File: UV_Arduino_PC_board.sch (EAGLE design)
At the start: 9 parts

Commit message: Added circuit board
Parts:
- removed X4: (no value), con-wago-500:W237-102
- added X5: (no value), con-wago-508:W237-04P
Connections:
- new net N$10: JP1.15, JP2.4
- new net N$12: JP1.8, X5-3.KL
- new net N$13: JP1.7, X5-2.KL
- new net N$2: JP1.14, JP2.5
- new net N$5: JP1.11, X1-1.KL, X2-1.KL
- new net N$6: JP1.10, X2-3.KL
- new net N$7: JP1.9, X2-2.KL
- new net N$8: JP1.6, X1-3.KL
- new net N$9: JP1.5, X1-2.KL
- net +12V: now also JP3.1
- net +5V: now also JP1.16, X5-4.KL
- net GND: now also JP1.1, JP1.17, JP3.2, X5-1.KL
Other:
- note added: "18 - RST 17 - GND 16 - +5VDC 15 - Arduino 0 RX 14 - Arduino 1 TX 13 - Arduino 2 12 - Arduino 3 11 - Arduino 4 Motor ENABLE -> SHB both EA 10 - Arduino 5 Left motor F -> SHB 0 PA 9 - Arduino 6 Left motor R -> SHB 0 PB 8 - Arduino 7 Platform UP / ~DOWN 7 - Arduino 8 Platform motion ENABLE 6 - Arduino 9 Right motor F -> SHB 1 PA 5 - Arduino 10 Right motor R -> SHB 1 PB 4 - Arduino 11 3 - Arduino 12 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"
- note added: "2 - GND 1 - Vin +12VDC to Arduino"
- note added: "BBB Arduino with jumper PRJ set for EXT"
- note added: "INPUT"
- note added: "OUTPUT"
- note added: "Pneumatics Control 4 - +5VDC 3 - UP / ~DOWN 2 - ENABLE 1 - GND"
- note removed: "BBB Arduino with jumper PRJ set for 5V"
- moved on the sheet: JP1, JP2, JP3, X1-1, X1-2, X1-3, X2-1, X2-2, X2-3

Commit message: Added name to schematic
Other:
- note added: "1.0"
- note added: "Author: Charles B. Malloch, PhD"
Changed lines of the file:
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@@
 2 - ENABLE
 1 - GND</text>
+<text x="162.56" y="12.7" size="2.54" layer="94" font="vector">Author: Charles B. Malloch, PhD</text>
+<text x="251.46" y="-7.62" size="2.54" layer="94" font="vector">1.0</text>
 </plain>
 <instances>

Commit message: Changed layout to fit actual board
Added change order to allow for a string of LEDs
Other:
- note added: "Change order: Add a connector for a string of neopixels or other addressable RGB LEDs - comm pins and 12V? power"
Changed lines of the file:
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@@
 <text x="162.56" y="12.7" size="2.54" layer="94" font="vector">Author: Charles B. Malloch, PhD</text>
 <text x="251.46" y="-7.62" size="2.54" layer="94" font="vector">1.0</text>
+<text x="45.72" y="-45.72" size="5.08" layer="94">Change order:
+Add a connector for a string of neopixels or other
+addressable RGB LEDs - comm pins and 12V? power</text>
 </plain>
 <instances>

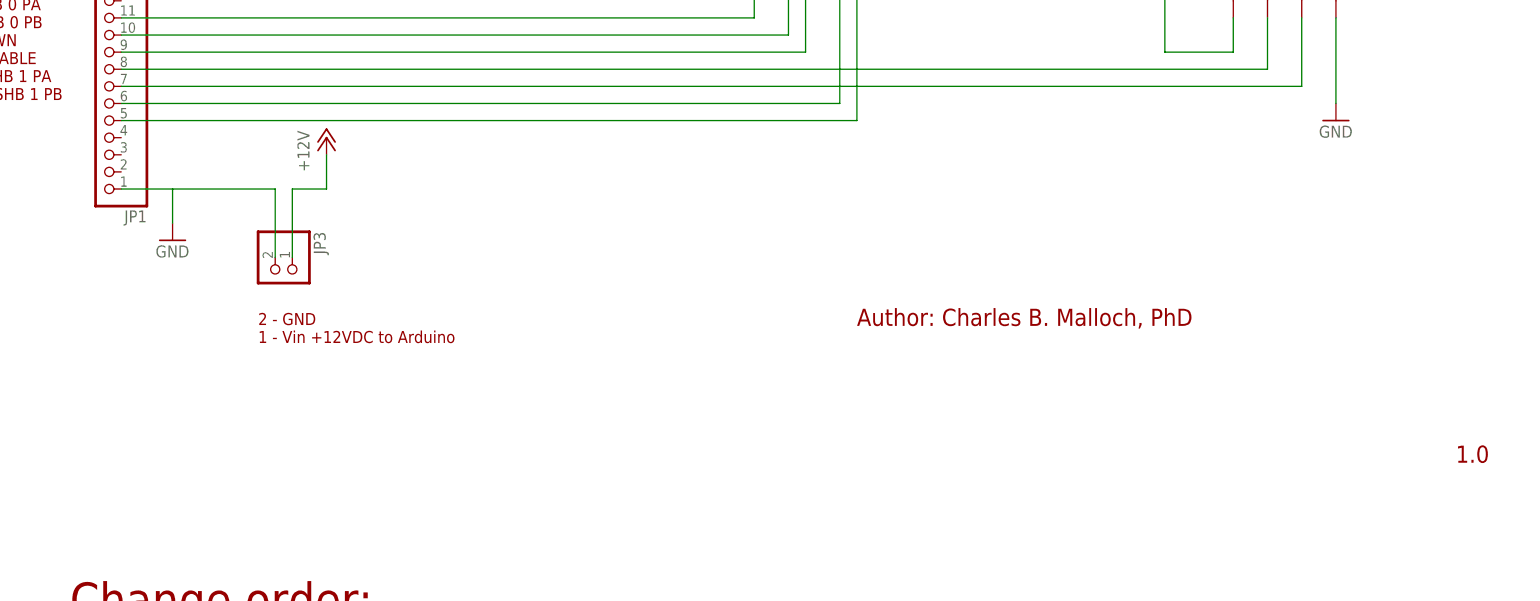
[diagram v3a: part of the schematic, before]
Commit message: Added lights control terminals
to control a LED strip with WS2811 or WS2812 controlled individually
addressable LEDs
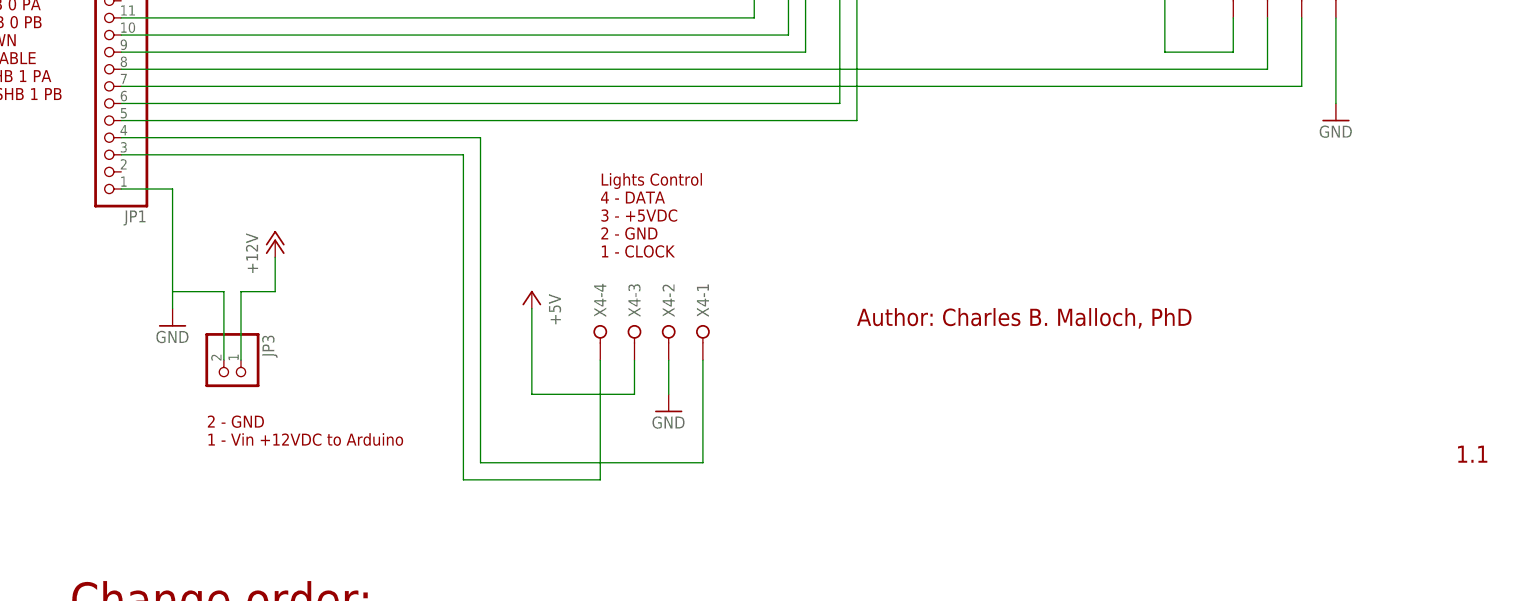
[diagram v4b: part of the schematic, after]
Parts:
- added X4: (no value), con-wago-508:W237-04P
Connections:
- new net N$3: JP1.4, X4-1.KL
- new net N$4: JP1.3, X4-4.KL
- net +5V: now also X4-3.KL
- net GND: now also X4-2.KL
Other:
- note added: "1.1"
- note added: "Lights Control 4 - DATA 3 - +5VDC 2 - GND 1 - CLOCK"
- note removed: "1.0"
- moved on the sheet: JP3
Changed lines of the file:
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@@
 <part name="GND6" library="supply1" deviceset="GND" device=""/>
 <part name="P+6" library="supply1" deviceset="+5V" device=""/>
+<part name="X4" library="con-wago-508" deviceset="W237-04P" device=""/>
+<part name="GND7" library="supply1" deviceset="GND" device=""/>
+<part name="P+7" library="supply1" deviceset="+5V" device=""/>
 </parts>
 <sheets>
@@
   2 - Arduino 13
   1 - GND</text>
-<text x="73.66" y="10.16" size="1.778" layer="94">2 - GND
+<text x="66.04" y="-5.08" size="1.778" layer="94">2 - GND
 1 - Vin +12VDC to Arduino</text>
 <text x="50.8" y="157.48" size="1.778" layer="94">INPUT</text>
@@
 1 - GND</text>
 <text x="162.56" y="12.7" size="2.54" layer="94" font="vector">Author: Charles B. Malloch, PhD</text>
-<text x="251.46" y="-7.62" size="2.54" layer="94" font="vector">1.0</text>
+<text x="251.46" y="-7.62" size="2.54" layer="94" font="vector">1.1</text>
 <text x="45.72" y="-45.72" size="5.08" layer="94">Change order:
 Add a connector for a string of neopixels or other
 addressable RGB LEDs - comm pins and 12V? power</text>
+<text x="124.46" y="22.86" size="1.778" layer="94">Lights Control
+4 - DATA
+3 - +5VDC
+2 - GND
+1 - CLOCK</text>
 </plain>
 <instances>
 <instance part="JP1" gate="A" x="50.8" y="53.34" rot="R180"/>
 <instance part="JP2" gate="A" x="152.4" y="152.4"/>
-<instance part="JP3" gate="G$1" x="76.2" y="20.32" rot="R270"/>
+<instance part="JP3" gate="G$1" x="68.58" y="5.08" rot="R270"/>
 <instance part="X1" gate="-1" x="170.18" y="83.82" rot="R180"/>
 <instance part="X1" gate="-2" x="170.18" y="88.9" rot="R180"/>
@@
 <instance part="GND3" gate="1" x="132.08" y="142.24"/>
 <instance part="P+4" gate="1" x="71.12" y="81.28" rot="MR0"/>
-<instance part="GND4" gate="1" x="60.96" y="25.4"/>
+<instance part="GND4" gate="1" x="60.96" y="12.7"/>
 <instance part="X5" gate="-1" x="233.68" y="63.5" rot="R270"/>
 <instance part="X5" gate="-2" x="228.6" y="63.5" rot="R270"/>
 <instance part="X5" gate="-3" x="223.52" y="63.5" rot="R270"/>
 <instance part="X5" gate="-4" x="218.44" y="63.5" rot="R270"/>
-<instance part="P+5" gate="1" x="83.82" y="40.64"/>
+<instance part="P+5" gate="1" x="76.2" y="25.4"/>
 <instance part="GND5" gate="1" x="66.04" y="76.2"/>
 <instance part="GND6" gate="1" x="233.68" y="43.18"/>
 <instance part="P+6" gate="1" x="208.28" y="68.58" rot="MR0"/>
+<instance part="X4" gate="-1" x="139.7" y="12.7" rot="R270"/>
+<instance part="X4" gate="-2" x="134.62" y="12.7" rot="R270"/>
+<instance part="X4" gate="-3" x="129.54" y="12.7" rot="R270"/>
+<instance part="X4" gate="-4" x="124.46" y="12.7" rot="R270"/>
+<instance part="GND7" gate="1" x="134.62" y="0"/>
+<instance part="P+7" gate="1" x="114.3" y="17.78" rot="MR0"/>
 </instances>
 <busses>
@@
 <pinref part="GND4" gate="1" pin="GND"/>
 <wire x1="53.34" y1="33.02" x2="60.96" y2="33.02" width="0.1524" layer="91"/>
-<wire x1="60.96" y1="33.02" x2="60.96" y2="27.94" width="0.1524" layer="91"/>
+<wire x1="60.96" y1="33.02" x2="60.96" y2="17.78" width="0.1524" layer="91"/>
+<wire x1="60.96" y1="17.78" x2="60.96" y2="15.24" width="0.1524" layer="91"/>
 <pinref part="JP3" gate="G$1" pin="2"/>
-<wire x1="76.2" y1="22.86" x2="76.2" y2="33.02" width="0.1524" layer="91"/>
-<wire x1="76.2" y1="33.02" x2="60.96" y2="33.02" width="0.1524" layer="91"/>
+<wire x1="68.58" y1="7.62" x2="68.58" y2="17.78" width="0.1524" layer="91"/>
+<wire x1="68.58" y1="17.78" x2="60.96" y2="17.78" width="0.1524" layer="91"/>
 </segment>
 <segment>
@@
 <pinref part="GND6" gate="1" pin="GND"/>
 <wire x1="233.68" y1="58.42" x2="233.68" y2="45.72" width="0.1524" layer="91"/>
+</segment>
+<segment>
+<pinref part="X4" gate="-2" pin="KL"/>
+<pinref part="GND7" gate="1" pin="GND"/>
+<wire x1="134.62" y1="7.62" x2="134.62" y2="2.54" width="0.1524" layer="91"/>
 </segment>
 </net>
@@
 <segment>
 <pinref part="JP3" gate="G$1" pin="1"/>
-<wire x1="78.74" y1="22.86" x2="78.74" y2="33.02" width="0.1524" layer="91"/>
+<wire x1="71.12" y1="7.62" x2="71.12" y2="17.78" width="0.1524" layer="91"/>
 <pinref part="P+5" gate="1" pin="+12V"/>
-<wire x1="78.74" y1="33.02" x2="83.82" y2="33.02" width="0.1524" layer="91"/>
-<wire x1="83.82" y1="33.02" x2="83.82" y2="38.1" width="0.1524" layer="91"/>
+<wire x1="71.12" y1="17.78" x2="76.2" y2="17.78" width="0.1524" layer="91"/>
+<wire x1="76.2" y1="17.78" x2="76.2" y2="22.86" width="0.1524" layer="91"/>
 </segment>
 </net>
@@
 <wire x1="218.44" y1="53.34" x2="208.28" y2="53.34" width="0.1524" layer="91"/>
 <wire x1="208.28" y1="53.34" x2="208.28" y2="66.04" width="0.1524" layer="91"/>
+</segment>
+<segment>
+<pinref part="P+7" gate="1" pin="+5V"/>
+<wire x1="114.3" y1="2.54" x2="114.3" y2="15.24" width="0.1524" layer="91"/>
+<pinref part="X4" gate="-3" pin="KL"/>
+<wire x1="114.3" y1="2.54" x2="129.54" y2="2.54" width="0.1524" layer="91"/>
+<wire x1="129.54" y1="2.54" x2="129.54" y2="7.62" width="0.1524" layer="91"/>
 </segment>
 </net>
@@
 </segment>
 </net>
+<net name="N$3" class="0">
+<segment>
+<pinref part="JP1" gate="A" pin="4"/>
+<wire x1="53.34" y1="40.64" x2="106.68" y2="40.64" width="0.1524" layer="91"/>
+<wire x1="106.68" y1="40.64" x2="106.68" y2="-7.62" width="0.1524" layer="91"/>
+<pinref part="X4" gate="-1" pin="KL"/>
+<wire x1="106.68" y1="-7.62" x2="139.7" y2="-7.62" width="0.1524" layer="91"/>
+<wire x1="139.7" y1="-7.62" x2="139.7" y2="7.62" width="0.1524" layer="91"/>
+</segment>
+</net>
+<net name="N$4" class="0">
+<segment>
+<pinref part="JP1" gate="A" pin="3"/>
+<wire x1="53.34" y1="38.1" x2="104.14" y2="38.1" width="0.1524" layer="91"/>
+<wire x1="104.14" y1="38.1" x2="104.14" y2="-10.16" width="0.1524" layer="91"/>
+<pinref part="X4" gate="-4" pin="KL"/>
+<wire x1="104.14" y1="-10.16" x2="124.46" y2="-10.16" width="0.1524" layer="91"/>
+<wire x1="124.46" y1="-10.16" x2="124.46" y2="7.62" width="0.1524" layer="91"/>
+</segment>
+</net>

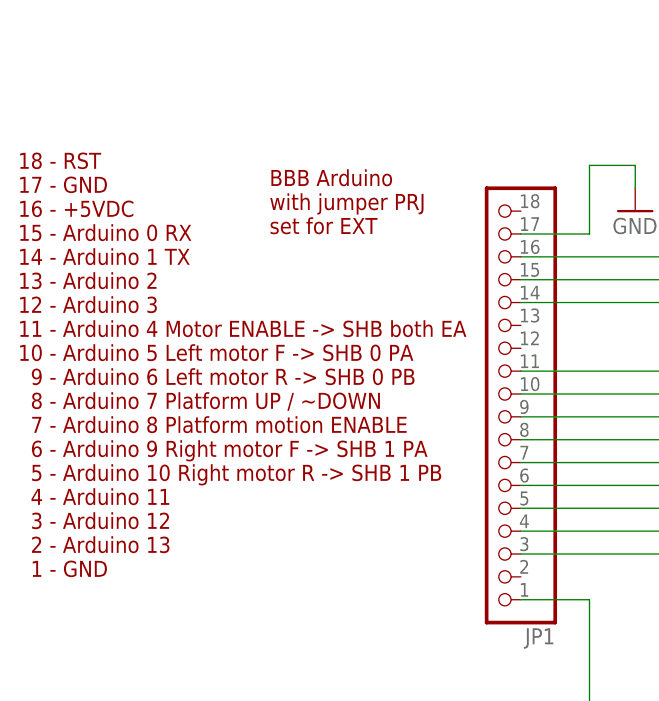
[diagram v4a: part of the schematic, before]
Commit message: Files now in Eagle v7.1.0 format
fixed some comments and adjusted to match the actual build.
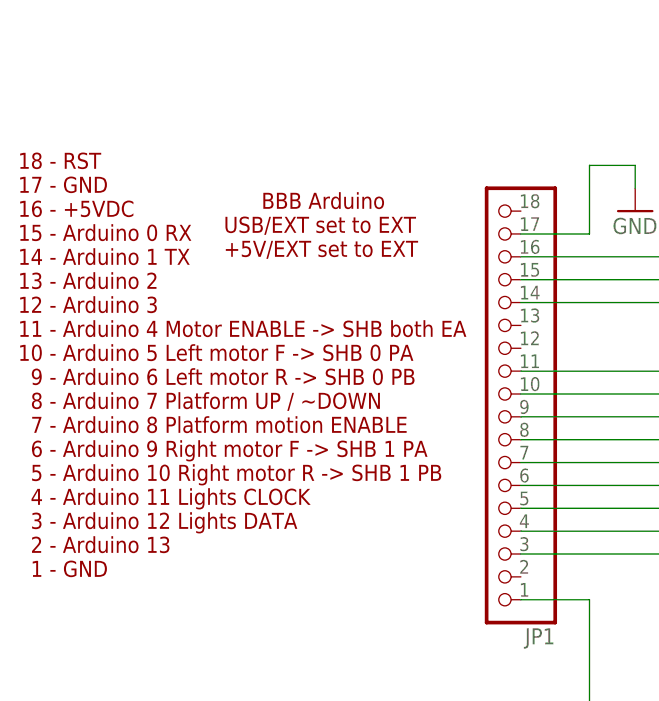
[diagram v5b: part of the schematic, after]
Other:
- note added: "18 - RST 17 - GND 16 - +5VDC 15 - Arduino 0 RX 14 - Arduino 1 TX 13 - Arduino 2 12 - Arduino 3 11 - Arduino 4 Motor ENABLE -> SHB both EA 10 - Arduino 5 Left motor F -> SHB 0 PA 9 - Arduino 6 Left motor R -> SHB 0 PB 8 - Arduino 7 Platform UP / ~DOWN 7 - Arduino 8 Platform motion ENABLE 6 - Arduino 9 Right motor F -> SHB 1 PA 5 - Arduino 10 Right motor R -> SHB 1 PB 4 - Arduino 11 Lights CLOCK 3 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"
- note added: "BBB Arduino USB/EXT set to EXT +5V/EXT set to EXT"
- note removed: "18 - RST 17 - GND 16 - +5VDC 15 - Arduino 0 RX 14 - Arduino 1 TX 13 - Arduino 2 12 - Arduino 3 11 - Arduino 4 Motor ENABLE -> SHB both EA 10 - Arduino 5 Left motor F -> SHB 0 PA 9 - Arduino 6 Left motor R -> SHB 0 PB 8 - Arduino 7 Platform UP / ~DOWN 7 - Arduino 8 Platform motion ENABLE 6 - Arduino 9 Right motor F -> SHB 1 PA 5 - Arduino 10 Right motor R -> SHB 1 PB 4 - Arduino 11 3 - Arduino 12 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"
- note removed: "BBB Arduino with jumper PRJ set for EXT"
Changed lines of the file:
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@@
 <?xml version="1.0" encoding="utf-8"?>
 <!DOCTYPE eagle SYSTEM "eagle.dtd">
-<eagle version="6.5.0">
+<eagle version="7.1.0">
 <drawing>
 <settings>
@@
 2 - H-Bridge (R) 1 PB
 1 - H-Bridge (R) 1 EA</text>
-<text x="25.4" y="73.66" size="1.778" layer="94">BBB Arduino
-with jumper PRJ
-set for EXT</text>
+<text x="20.32" y="71.12" size="1.778" layer="94">      BBB Arduino
+USB/EXT set to EXT
++5V/EXT set to EXT</text>
 <text x="58.42" y="129.54" size="1.778" layer="94">DC-DC Buck Converter
 set for 12V output</text>
@@
   6 - Arduino 9 Right motor F -&gt; SHB 1 PA
   5 - Arduino 10 Right motor R -&gt; SHB 1 PB
-  4 - Arduino 11
-  3 - Arduino 12
+  4 - Arduino 11 Lights CLOCK
+  3 - Arduino 12 Lights DATA
   2 - Arduino 13
   1 - GND</text>

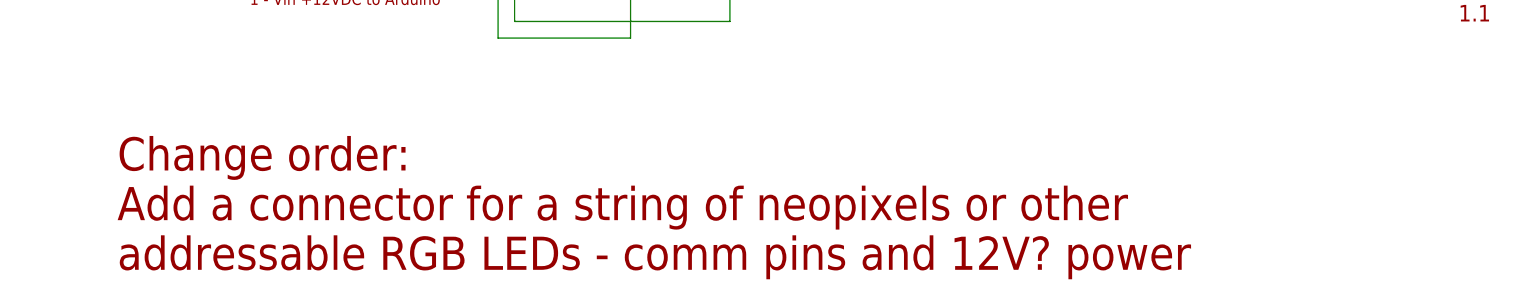
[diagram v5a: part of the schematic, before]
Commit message: Add connector for neopixels
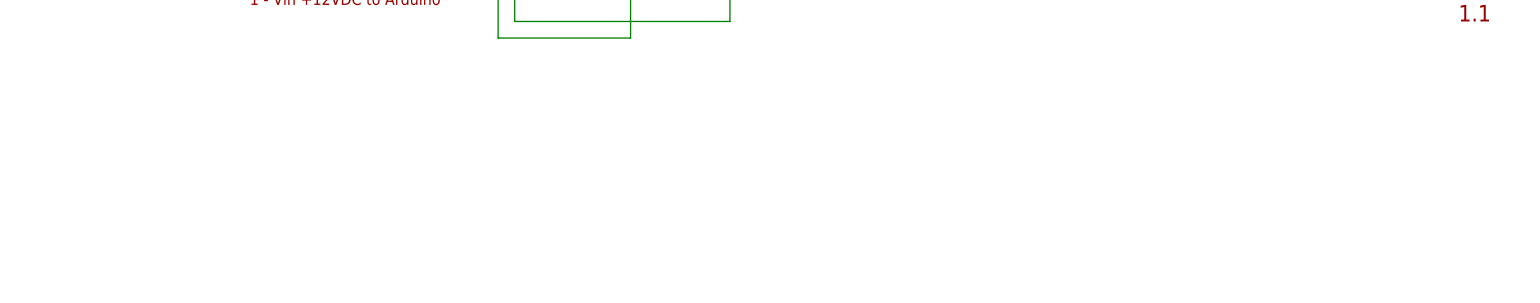
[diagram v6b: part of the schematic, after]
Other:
- note removed: "Change order: Add a connector for a string of neopixels or other addressable RGB LEDs - comm pins and 12V? power"
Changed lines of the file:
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@@
 <text x="162.56" y="12.7" size="2.54" layer="94" font="vector">Author: Charles B. Malloch, PhD</text>
 <text x="251.46" y="-7.62" size="2.54" layer="94" font="vector">1.1</text>
-<text x="45.72" y="-45.72" size="5.08" layer="94">Change order:
-Add a connector for a string of neopixels or other
-addressable RGB LEDs - comm pins and 12V? power</text>
 <text x="124.46" y="22.86" size="1.778" layer="94">Lights Control
 4 - DATA
